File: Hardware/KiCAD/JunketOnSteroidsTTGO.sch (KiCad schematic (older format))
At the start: 29 parts, among them J1 To PSU host board, J2 To PSU host board, J3 Serial, J4 ESP32-TFT, J5 ESP32-TFT, J6 NRST/SWIM

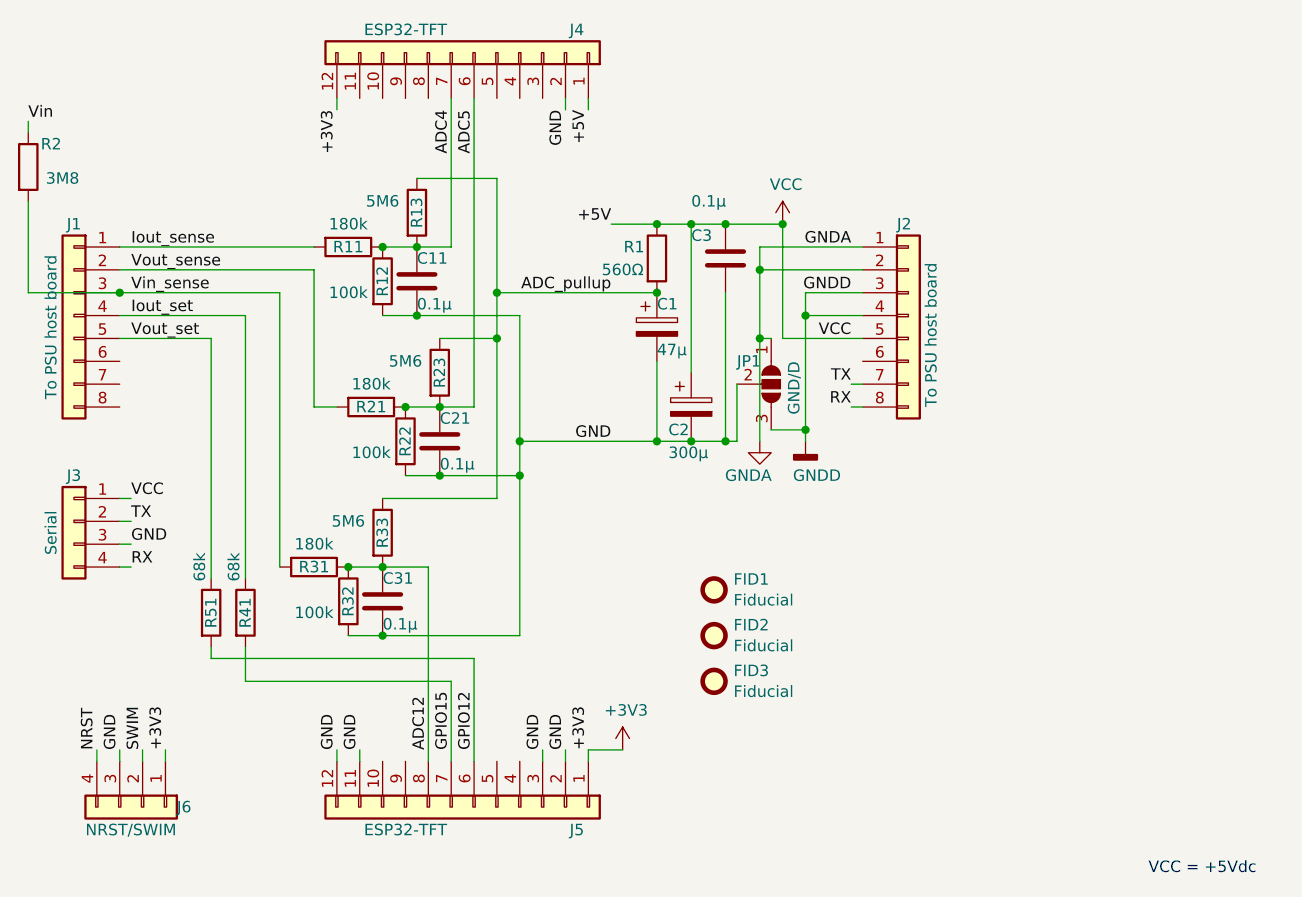
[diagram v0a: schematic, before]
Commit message: Swap GPIO12 & 15, Add !ON with solder-option, Replace SWIM with I2C
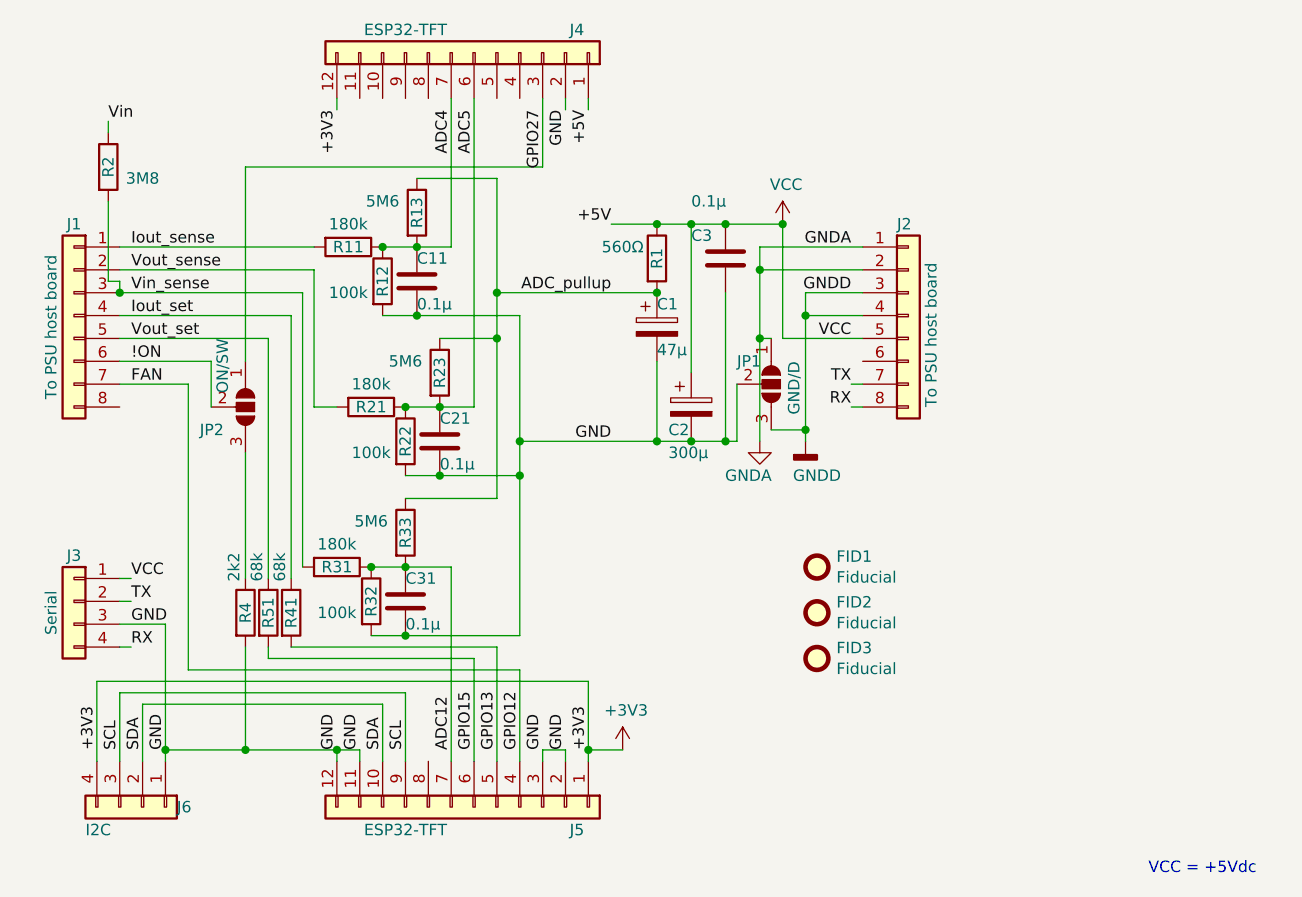
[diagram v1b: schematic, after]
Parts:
- added JP2: ON/SW, Jumper:SolderJumper-3_P1.3mm_Open_RoundedPad1.0x1.5mm, symbol Jumper:SolderJumper_3_Open
- added R4: 2k2, Resistor_THT:R_Axial_DIN0204_L3.6mm_D1.6mm_P7.62mm_Horizontal, symbol Device:R
- J6: value NRST/SWIM -> I2C
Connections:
- net GPIO12 is gone; now on net GPIO15: J5.6 (Pin_6), R51.2
- net NRST is gone; now on net +3V3: J6.4 (Pin_4)
- net SWIM is gone; now on net SDA: J6.2 (Pin_2)
- net +3V3: no longer J6.1 (Pin_1)
- net ADC12: now also J5.7 (Pin_7); no longer J5.8 (Pin_8)
- net GND: now also J6.1 (Pin_1), R4.2; no longer J6.3 (Pin_3)
- net GPIO15: no longer J5.7 (Pin_7), R41.2
- net !ON: now reaches J1.6 (Pin_6)
- net !ON: now also JP2.2 (C)
- net FAN: now reaches J1.7 (Pin_7)
- net FAN: now also J5.4 (Pin_4)
- net GPIO27: now reaches J4.3 (Pin_3)
- net GPIO27: now also JP2.1 (A)
- net SDA: now reaches J5.10 (Pin_10)
- net GPIO13: now reaches J5.5 (Pin_5)
- net GPIO13: now also R41.2
- net SCL: now reaches J5.9 (Pin_9)
- net SCL: now also J6.3 (Pin_3)
- new net: JP2.3 (B), R4.1
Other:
- moved on the sheet: C31, FID1, FID2, FID3, J3, R2, R31, R32, R33, R41, R51

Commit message: Rev 0.3
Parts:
- added JP3: Vin_sense, Jumper:SolderJumper-3_P1.3mm_Open_RoundedPad1.0x1.5mm, symbol Jumper:SolderJumper_3_Open
- added TP1: Vin_sense, Connector_Wire:SolderWire-0.1sqmm_1x01_D0.4mm_OD1mm, symbol Connector:TestPoint
- J3, J6: footprint Connector_PinHeader_2.54mm:PinHeader_1x04_P2.54mm_Vertical -> Connector_PinHeader_2.54mm:PinHeader_1x04_P2.54mm_Horizontal
- renumbered R2 to R34, R4 to R6
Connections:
- net +3V3: now also J6.1 (Pin_1); no longer J6.4 (Pin_4)
- net GND: now also J6.2 (Pin_2); no longer J6.1 (Pin_1)
- net SDA: now also J6.4 (Pin_4); no longer J6.2 (Pin_2)
- net Vin: now also TP1.1
- net Vin_sense: now also JP3.1 (A); no longer R31.2, R34.2
- new net: JP3.2 (C), R31.2
- new net: JP3.3 (B), R34.2
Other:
- moved on the sheet: C1, C11, C2, C21, C3, C31, FID1, FID2, FID3, J1, J2, J3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
